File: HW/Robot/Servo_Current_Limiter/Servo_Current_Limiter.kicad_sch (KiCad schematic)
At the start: 2 parts, among them J11 1x2 2.54mm male

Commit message: Sch update.
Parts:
- added C1: 100n, For_Rasterboard:C_Disc_D3.0mm_W1.6mm_P5.00mm, symbol Device:C
- added J2: Conn_02x05_Odd_Even, Connector_PinSocket_2.54mm:PinSocket_2x05_P2.54mm_Vertical, symbol Connector_Generic:Conn_02x05_Odd_Even
- added JP1: 1x2 2.54mm male, Connector_PinHeader_2.54mm:PinHeader_1x02_P2.54mm_Vertical, symbol Jumper:Jumper_2_Open
- added U1: LM324, Package_DIP:DIP-14_W7.62mm, symbol Amplifier_Operational:LM324
- renumbered J11 to J1
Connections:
- net +5V: now also C1.1, JP1.2 (B), U1.4 (V+); no longer A1.5 (+5V)
- net DIS0: no longer A1.17 (D2)
- net GND: now also C1.2, J2.10 (Pin_10), J2.9 (Pin_9), U1.11 (V-)
- net OUT1: now reaches A1.10 (A1)
- net OUT2: now reaches A1.11 (A2)
- net OUT3: now reaches A1.12 (A3)
- net ARD_PWM3: now reaches A1.20 (D5)
- net ARD_PWM3: now also J2.7 (Pin_7)
- net ARD_PWM2: now reaches A1.24 (D9)
- net ARD_PWM2: now also J2.5 (Pin_5)
- net ARD_PWM1: now reaches A1.25 (D10)
- net ARD_PWM1: now also J2.3 (Pin_3)
- net ARD_PWM0: now reaches A1.26 (D11)
- net ARD_PWM0: now also J2.1 (Pin_1)
- new net: A1.5 (+5V), JP1.1 (A)
- new net PWM0: J2.2 (Pin_2)
- new net PWM1: J2.4 (Pin_4)
- new net PWM2: J2.6 (Pin_6)
- new net PWM3: J2.8 (Pin_8)
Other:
- added sheet ch1 (channel.kicad_sch)
- added sheet ch2 (channel.kicad_sch)
- added sheet ch3 (channel.kicad_sch)
- sheet ch0 ports: added PWM; removed none

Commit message: PCB for 1 channel done.
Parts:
- C1: footprint For_Rasterboard:C_Disc_D3.0mm_W1.6mm_P5.00mm -> For_Rasterboard:C_Disc_D3.0mm_W1.6mm_P2.50mm
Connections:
- net ARD_PWM0: now also J2.2 (Pin_2); no longer J2.1 (Pin_1)
- net ARD_PWM1: now also J2.4 (Pin_4); no longer J2.3 (Pin_3)
- net ARD_PWM2: now also J2.6 (Pin_6); no longer J2.5 (Pin_5)
- net ARD_PWM3: now also J2.8 (Pin_8); no longer J2.7 (Pin_7)
- net DIS0: now also A1.17 (D2)
- net PWM0: now also J2.1 (Pin_1); no longer J2.2 (Pin_2)
- net PWM1: now also J2.3 (Pin_3); no longer J2.4 (Pin_4)
- net PWM2: now also J2.5 (Pin_5); no longer J2.6 (Pin_6)
- net PWM3: now also J2.7 (Pin_7); no longer J2.8 (Pin_8)
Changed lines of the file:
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@@
     (stroke (width 0) (type default) (color 0 0 0 0))
   )
-  (wire (pts (xy 94.615 120.015) (xy 100.965 120.015))
+  (wire (pts (xy 104.14 119.38) (xy 110.49 119.38))
     (stroke (width 0) (type default) (color 0 0 0 0))
   )
@@
     (effects (font (size 1.27 1.27)) (justify left bottom))
   )
-  (label "DIS0" (at 94.615 120.015 0)
+  (label "DIS0" (at 104.14 119.38 0)
     (effects (font (size 1.27 1.27)) (justify left bottom))
   )
@@
     (pin "1")
   )
-  (symbol (lib_id "Connector_Generic:Conn_02x05_Odd_Even") (at 132.715 45.085 0) (unit 1)
+  (symbol (lib_id "Connector_Generic:Conn_02x05_Odd_Even") (at 135.255 45.085 0) (mirror y) (unit 1)
     (in_bom yes) (on_board yes) (fields_autoplaced)
     (property "Reference" "J2" (id 0) (at 133.985 33.02 0))
     (property "Value" "Conn_02x05_Odd_Even" (id 1) (at 133.985 35.56 0))
-    (property "Footprint" "Connector_PinSocket_2.54mm:PinSocket_2x05_P2.54mm_Vertical" (id 2) (at 132.715 45.085 0)
-      (effects (font (size 1.27 1.27)) hide)
-    )
-    (property "Datasheet" "~" (id 3) (at 132.715 45.085 0)
+    (property "Footprint" "Connector_PinSocket_2.54mm:PinSocket_2x05_P2.54mm_Vertical" (id 2) (at 135.255 45.085 0)
+      (effects (font (size 1.27 1.27)) hide)
+    )
+    (property "Datasheet" "~" (id 3) (at 135.255 45.085 0)
       (effects (font (size 1.27 1.27)) hide)
     )
@@
     (property "Reference" "C1" (id 0) (at 182.245 86.36 90))
     (property "Value" "100n" (id 1) (at 182.245 88.9 90))
-    (property "Footprint" "For_Rasterboard:C_Disc_D3.0mm_W1.6mm_P5.00mm" (id 2) (at 178.435 94.9452 0)
+    (property "Footprint" "For_Rasterboard:C_Disc_D3.0mm_W1.6mm_P2.50mm" (id 2) (at 178.435 94.9452 0)
       (effects (font (size 1.27 1.27)) hide)
     )
@@
     )
     (path "/24d45924-f372-4739-95f6-4c73cb3a982f"
-      (reference "C1") (unit 1) (value "100n") (footprint "For_Rasterboard:C_Disc_D3.0mm_W1.6mm_P5.00mm")
+      (reference "C1") (unit 1) (value "100n") (footprint "For_Rasterboard:C_Disc_D3.0mm_W1.6mm_P2.50mm")
     )
     (path "/8142c135-dcaf-4e2d-b554-7b6845c7c442"
@@
     )
     (path "/18a28627-1db1-4a0b-947d-f716714df9ad/512a76b4-a486-43e5-b07f-9543c3ee410b"
-      (reference "R1") (unit 1) (value "220") (footprint "For_Rasterboard:R_Axial_DIN0207_L6.3mm_D2.5mm_Pinf_Horizontal")
+      (reference "R1") (unit 1) (value "220") (footprint "For_Rasterboard:R_Axial_DIN0207_L6.3mm_D2.5mm_P5.08mm_Vertical")
     )
     (path "/18a28627-1db1-4a0b-947d-f716714df9ad/ae57e91c-5723-4583-8728-3d29c638ab36"

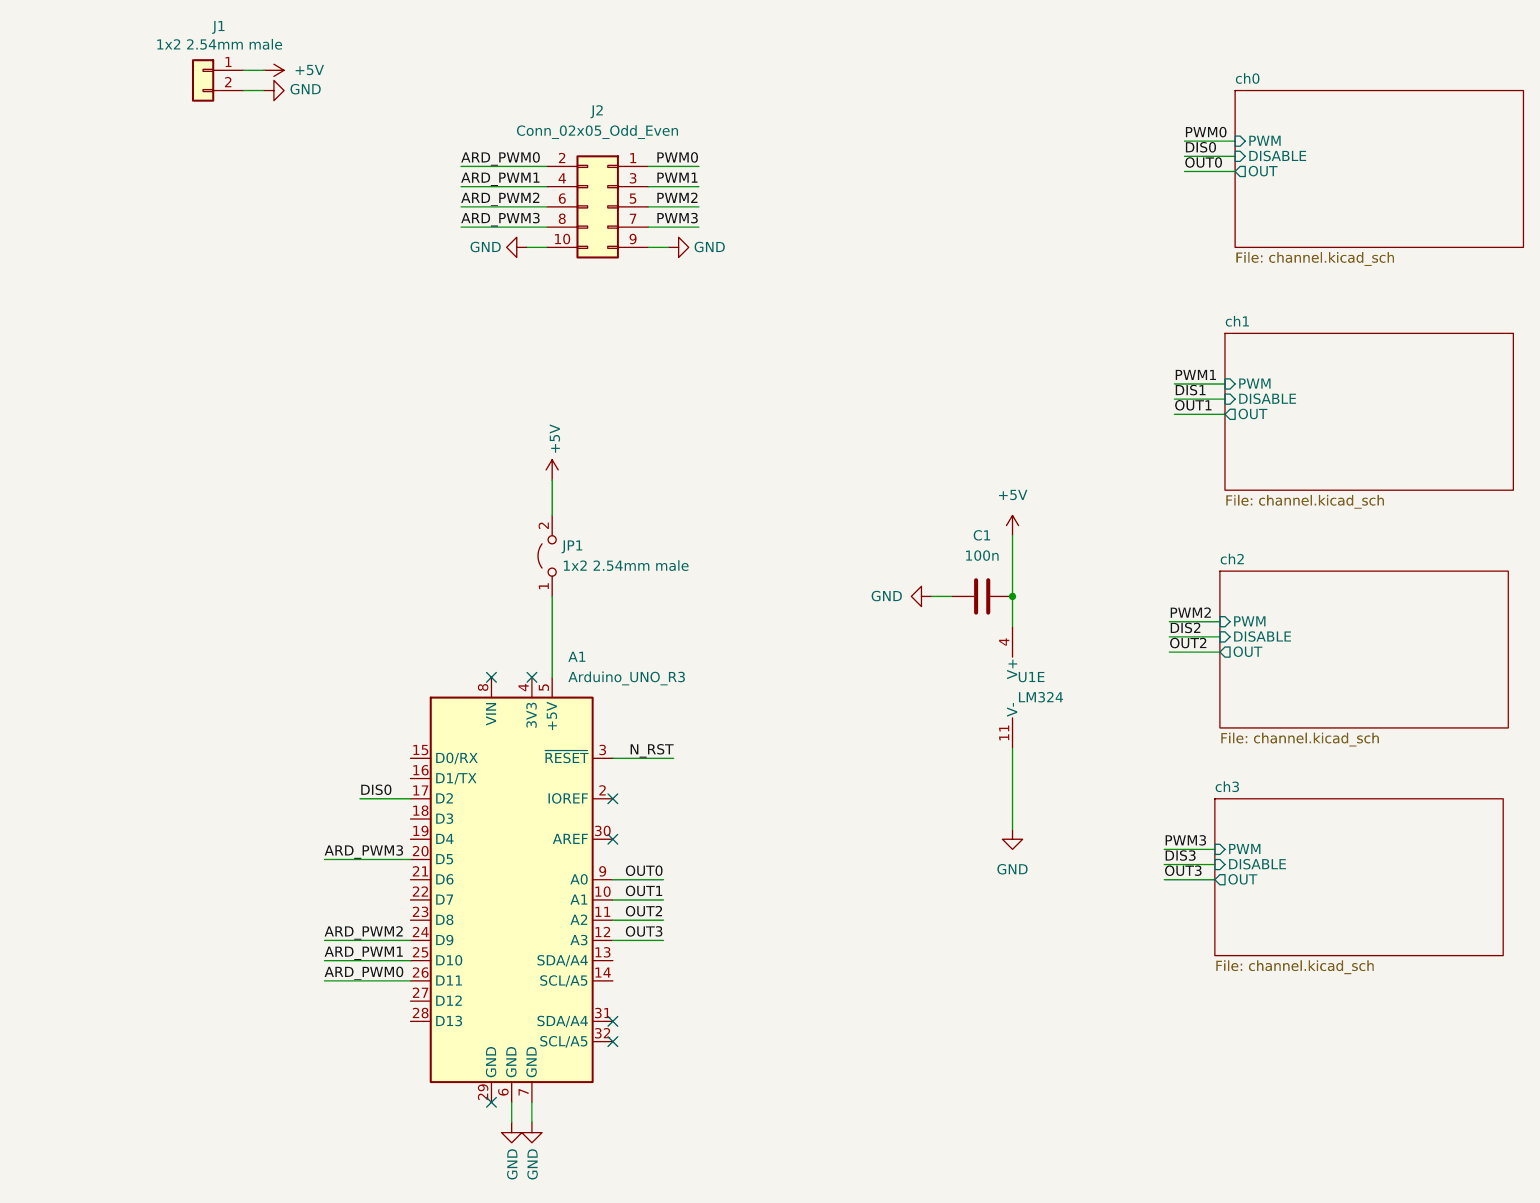
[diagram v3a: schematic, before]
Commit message: Dual power. Snapped to grid.
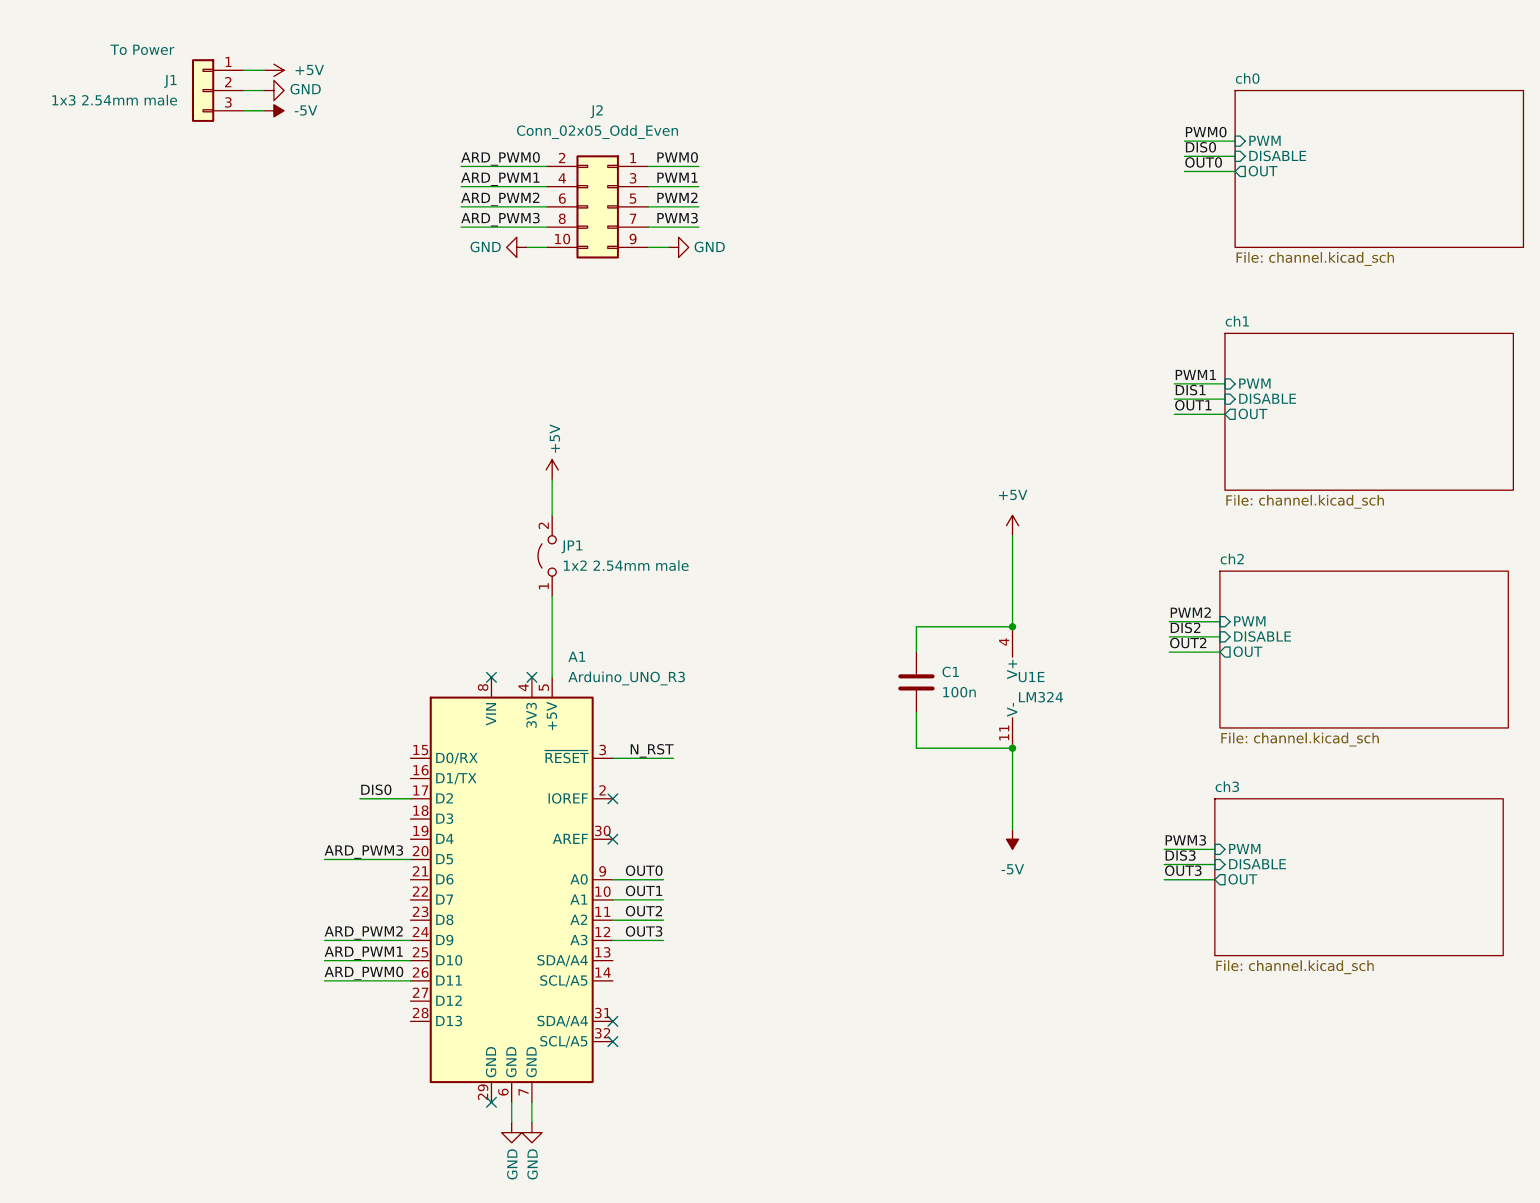
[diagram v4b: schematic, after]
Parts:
- removed J1: 1x2 2.54mm male, Extra_Common:MOLEX-22-23-2021, symbol Connector_Generic:Conn_01x02
- added J1: 1x3 2.54mm male, Connector_PinHeader_2.54mm:PinHeader_1x03_P2.54mm_Vertical, symbol Connector_Generic:Conn_01x03
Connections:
- net +5V: now also J1.1 (Pin_1)
- net GND: now also J1.2 (Pin_2); no longer C1.2, U1.11 (V-)
- new net -5V: C1.2, J1.3 (Pin_3), U1.11 (V-)
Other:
- moved on the sheet: C1
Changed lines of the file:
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@@
 (kicad_sch (version 20211123) (generator eeschema)
   (paper "A4")
-  (junction (at 186.055 93.98) (diameter 0) (color 0 0 0 0)
+  (junction (at 186.055 97.79) (diameter 0) (color 0 0 0 0)
+  )
+  (junction (at 186.055 113.03) (diameter 0) (color 0 0 0 0)
   )
   (no_connect (at 135.89 124.46))
@@
     (stroke (width 0) (type default) (color 0 0 0 0))
   )
+  (wire (pts (xy 173.99 100.965) (xy 173.99 97.79))
+    (stroke (width 0) (type default) (color 0 0 0 0))
+  )
   (wire (pts (xy 128.27 79.375) (xy 128.27 83.82))
     (stroke (width 0) (type default) (color 0 0 0 0))
@@
     (stroke (width 0) (type default) (color 0 0 0 0))
   )
+  (wire (pts (xy 173.99 108.585) (xy 173.99 113.03))
+    (stroke (width 0) (type default) (color 0 0 0 0))
+  )
+  (wire (pts (xy 173.99 97.79) (xy 186.055 97.79))
+    (stroke (width 0) (type default) (color 0 0 0 0))
+  )
   (wire (pts (xy 146.685 40.005) (xy 140.335 40.005))
     (stroke (width 0) (type default) (color 0 0 0 0))
@@
     (stroke (width 0) (type default) (color 0 0 0 0))
   )
-  (wire (pts (xy 186.055 86.36) (xy 186.055 93.98))
-    (stroke (width 0) (type default) (color 0 0 0 0))
-  )
-  (wire (pts (xy 186.055 93.98) (xy 186.055 97.79))
+  (wire (pts (xy 186.055 86.36) (xy 186.055 97.79))
     (stroke (width 0) (type default) (color 0 0 0 0))
   )
@@
     (stroke (width 0) (type default) (color 0 0 0 0))
   )
-  (wire (pts (xy 175.895 93.98) (xy 178.435 93.98))
-    (stroke (width 0) (type default) (color 0 0 0 0))
-  )
   (wire (pts (xy 205.105 129.54) (xy 211.455 129.54))
     (stroke (width 0) (type default) (color 0 0 0 0))
@@
     (stroke (width 0) (type default) (color 0 0 0 0))
   )
+  (wire (pts (xy 89.535 33.02) (xy 92.075 33.02))
+    (stroke (width 0) (type default) (color 0 0 0 0))
+  )
   (wire (pts (xy 127.635 50.165) (xy 125.095 50.165))
     (stroke (width 0) (type default) (color 0 0 0 0))
@@
   )
   (wire (pts (xy 92.075 30.48) (xy 89.535 30.48))
+    (stroke (width 0) (type default) (color 0 0 0 0))
+  )
+  (wire (pts (xy 173.99 113.03) (xy 186.055 113.03))
     (stroke (width 0) (type default) (color 0 0 0 0))
   )
@@
     (pin "9")
   )
-  (symbol (lib_id "Device:C") (at 182.245 93.98 270) (unit 1)
-    (in_bom yes) (on_board yes) (fields_autoplaced)
-    (property "Reference" "C1" (id 0) (at 182.245 86.36 90))
-    (property "Value" "100n" (id 1) (at 182.245 88.9 90))
-    (property "Footprint" "For_Rasterboard:C_Disc_D3.0mm_W1.6mm_P2.50mm" (id 2) (at 178.435 94.9452 0)
-      (effects (font (size 1.27 1.27)) hide)
-    )
-    (property "Datasheet" "~" (id 3) (at 182.245 93.98 0)
+  (symbol (lib_id "power:-5V") (at 186.055 123.19 180) (unit 1)
+    (in_bom yes) (on_board yes) (fields_autoplaced)
+    (property "Reference" "#PWR0105" (id 0) (at 186.055 125.73 0)
+      (effects (font (size 1.27 1.27)) hide)
+    )
+    (property "Value" "-5V" (id 1) (at 186.055 128.27 0))
+    (property "Footprint" "" (id 2) (at 186.055 123.19 0)
+      (effects (font (size 1.27 1.27)) hide)
+    )
+    (property "Datasheet" "" (id 3) (at 186.055 123.19 0)
+      (effects (font (size 1.27 1.27)) hide)
+    )
+    (pin "1")
+  )
+  (symbol (lib_id "Device:C") (at 173.99 104.775 0) (unit 1)
+    (in_bom yes) (on_board yes) (fields_autoplaced)
+    (property "Reference" "C1" (id 0) (at 177.165 103.5049 0)
+      (effects (font (size 1.27 1.27)) (justify left))
+    )
+    (property "Value" "100n" (id 1) (at 177.165 106.0449 0)
+      (effects (font (size 1.27 1.27)) (justify left))
+    )
+    (property "Footprint" "For_Rasterboard:C_Disc_D3.0mm_W1.6mm_P2.50mm" (id 2) (at 174.9552 108.585 0)
+      (effects (font (size 1.27 1.27)) hide)
+    )
+    (property "Datasheet" "~" (id 3) (at 173.99 104.775 0)
       (effects (font (size 1.27 1.27)) hide)
     )
@@
     (pin "9")
   )
+  (symbol (lib_id "Connector_Generic:Conn_01x03") (at 84.455 30.48 0) (mirror y) (unit 1)
+    (in_bom yes) (on_board yes)
+    (property "Reference" "J1" (id 0) (at 81.28 29.2099 0)
+      (effects (font (size 1.27 1.27)) (justify left))
+    )
+    (property "Value" "1x3 2.54mm male" (id 1) (at 81.28 31.7499 0)
+      (effects (font (size 1.27 1.27)) (justify left))
+    )
+    (property "Footprint" "Connector_PinHeader_2.54mm:PinHeader_1x03_P2.54mm_Vertical" (id 2) (at 84.455 30.48 0)
+      (effects (font (size 1.27 1.27)) hide)
+    )
+    (property "Datasheet" "~" (id 3) (at 84.455 30.48 0)
+      (effects (font (size 1.27 1.27)) hide)
+    )
+    (property "Comment" "To Power" (id 4) (at 76.835 25.4 0))
+    (pin "1")
+    (pin "2")
+    (pin "3")
+  )
   (symbol (lib_id "power:+5V") (at 186.055 86.36 0) (unit 1)
     (in_bom yes) (on_board yes) (fields_autoplaced)
@@
     (pin "1")
   )
-  (symbol (lib_id "power:GND") (at 186.055 123.19 0) (unit 1)
-    (in_bom yes) (on_board yes) (fields_autoplaced)
-    (property "Reference" "#PWR010" (id 0) (at 186.055 129.54 0)
-      (effects (font (size 1.27 1.27)) hide)
-    )
-    (property "Value" "GND" (id 1) (at 186.055 128.27 0))
-    (property "Footprint" "" (id 2) (at 186.055 123.19 0)
-      (effects (font (size 1.27 1.27)) hide)
-    )
-    (property "Datasheet" "" (id 3) (at 186.055 123.19 0)
-      (effects (font (size 1.27 1.27)) hide)
-    )
-    (pin "1")
-  )
-  (symbol (lib_id "Connector_Generic:Conn_01x02") (at 84.455 27.94 0) (mirror y) (unit 1)
-    (in_bom yes) (on_board yes)
-    (property "Reference" "J1" (id 0) (at 86.487 22.4282 0))
-    (property "Value" "1x2 2.54mm male" (id 1) (at 86.487 24.7396 0))
-    (property "Footprint" "Extra_Common:MOLEX-22-23-2021" (id 2) (at 84.455 27.94 0)
-      (effects (font (size 1.27 1.27)) hide)
-    )
-    (property "Datasheet" "~" (id 3) (at 84.455 27.94 0)
-      (effects (font (size 1.27 1.27)) hide)
-    )
-    (pin "1")
-    (pin "2")
+  (symbol (lib_id "power:-5V") (at 92.075 33.02 270) (unit 1)
+    (in_bom yes) (on_board yes) (fields_autoplaced)
+    (property "Reference" "#PWR08" (id 0) (at 94.615 33.02 0)
+      (effects (font (size 1.27 1.27)) hide)
+    )
+    (property "Value" "-5V" (id 1) (at 95.885 33.0199 90)
+      (effects (font (size 1.27 1.27)) (justify left))
+    )
+    (property "Footprint" "" (id 2) (at 92.075 33.02 0)
+      (effects (font (size 1.27 1.27)) hide)
+    )
+    (property "Datasheet" "" (id 3) (at 92.075 33.02 0)
+      (effects (font (size 1.27 1.27)) hide)
+    )
+    (pin "1")
   )
   (symbol (lib_id "Jumper:Jumper_2_Open") (at 128.27 88.9 90) (unit 1)
@@
     )
     (property "Datasheet" "" (id 3) (at 92.075 30.48 0)
-      (effects (font (size 1.27 1.27)) hide)
-    )
-    (pin "1")
-  )
-  (symbol (lib_id "power:GND") (at 175.895 93.98 270) (unit 1)
-    (in_bom yes) (on_board yes)
-    (property "Reference" "#PWR08" (id 0) (at 169.545 93.98 0)
-      (effects (font (size 1.27 1.27)) hide)
-    )
-    (property "Value" "GND" (id 1) (at 168.275 93.98 90)
-      (effects (font (size 1.27 1.27)) (justify left))
-    )
-    (property "Footprint" "" (id 2) (at 175.895 93.98 0)
-      (effects (font (size 1.27 1.27)) hide)
-    )
-    (property "Datasheet" "" (id 3) (at 175.895 93.98 0)
       (effects (font (size 1.27 1.27)) hide)
     )
@@
       (reference "#PWR07") (unit 1) (value "GND") (footprint "")
     )
-    (path "/d0a5d107-898d-4441-aed7-6df680a4435d"
-      (reference "#PWR08") (unit 1) (value "GND") (footprint "")
+    (path "/829a5acd-f730-4ef5-aeae-50123d7984f6"
+      (reference "#PWR08") (unit 1) (value "-5V") (footprint "")
     )
     (path "/62043049-830f-4125-8172-bd9fb8bde481"
       (reference "#PWR09") (unit 1) (value "+5V") (footprint "")
     )
-    (path "/750e5c88-1d97-4efa-a42e-08a85b0d21a2"
-      (reference "#PWR010") (unit 1) (value "GND") (footprint "")
-    )
     (path "/18a28627-1db1-4a0b-947d-f716714df9ad/30b2f70b-b676-470e-8c96-0741314c5460"
       (reference "#PWR011") (unit 1) (value "+5V") (footprint "")
@@
       (reference "#PWR0104") (unit 1) (value "GND") (footprint "")
     )
+    (path "/1e10b1d3-7750-4dc0-92a0-ffde325c07d5"
+      (reference "#PWR0105") (unit 1) (value "-5V") (footprint "")
+    )
     (path "/3f820c47-2e2b-42fc-b572-02fb33521462"
       (reference "A1") (unit 1) (value "Arduino_UNO_R3") (footprint "For_Rasterboard:Arduino_UNO_R3_WithMountingHoles_Snapped_to_P2.54mm")
@@
       (reference "C1") (unit 1) (value "100n") (footprint "For_Rasterboard:C_Disc_D3.0mm_W1.6mm_P2.50mm")
     )
-    (path "/8142c135-dcaf-4e2d-b554-7b6845c7c442"
-      (reference "J1") (unit 1) (value "1x2 2.54mm male") (footprint "Extra_Common:MOLEX-22-23-2021")
+    (path "/48a85985-449b-4592-b9d3-0088a105595a"
+      (reference "J1") (unit 1) (value "1x3 2.54mm male") (footprint "Connector_PinHeader_2.54mm:PinHeader_1x03_P2.54mm_Vertical")
     )
     (path "/0bed8761-8178-45ff-a640-b103d2f699e5"
